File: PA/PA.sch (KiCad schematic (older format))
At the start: 80 parts, among them J1 Conn_Coaxial, J2 Conn_01x02, J27 Conn_01x01, J28 Conn_01x01, J3 Conn_Coaxial, J4 Conn_01x02, J5 Conn_01x02, J6 Conn_01x01, J7 Conn_01x01, J8 Conn_01x01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

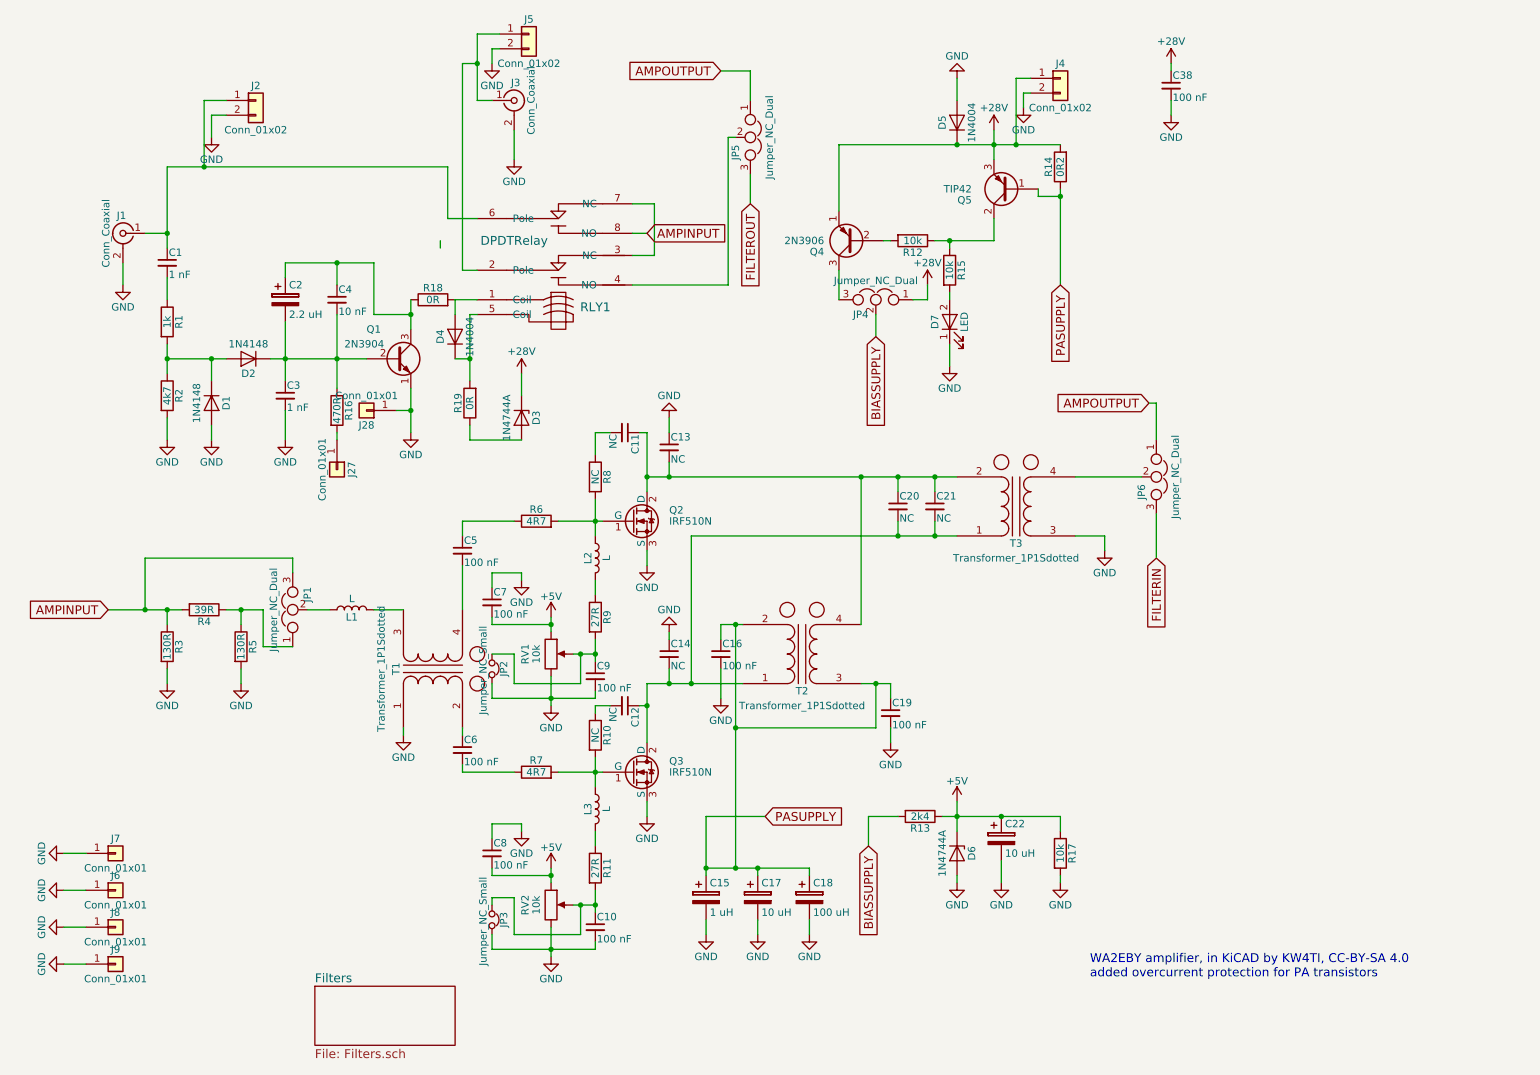
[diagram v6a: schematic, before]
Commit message: JLCPCB order tested
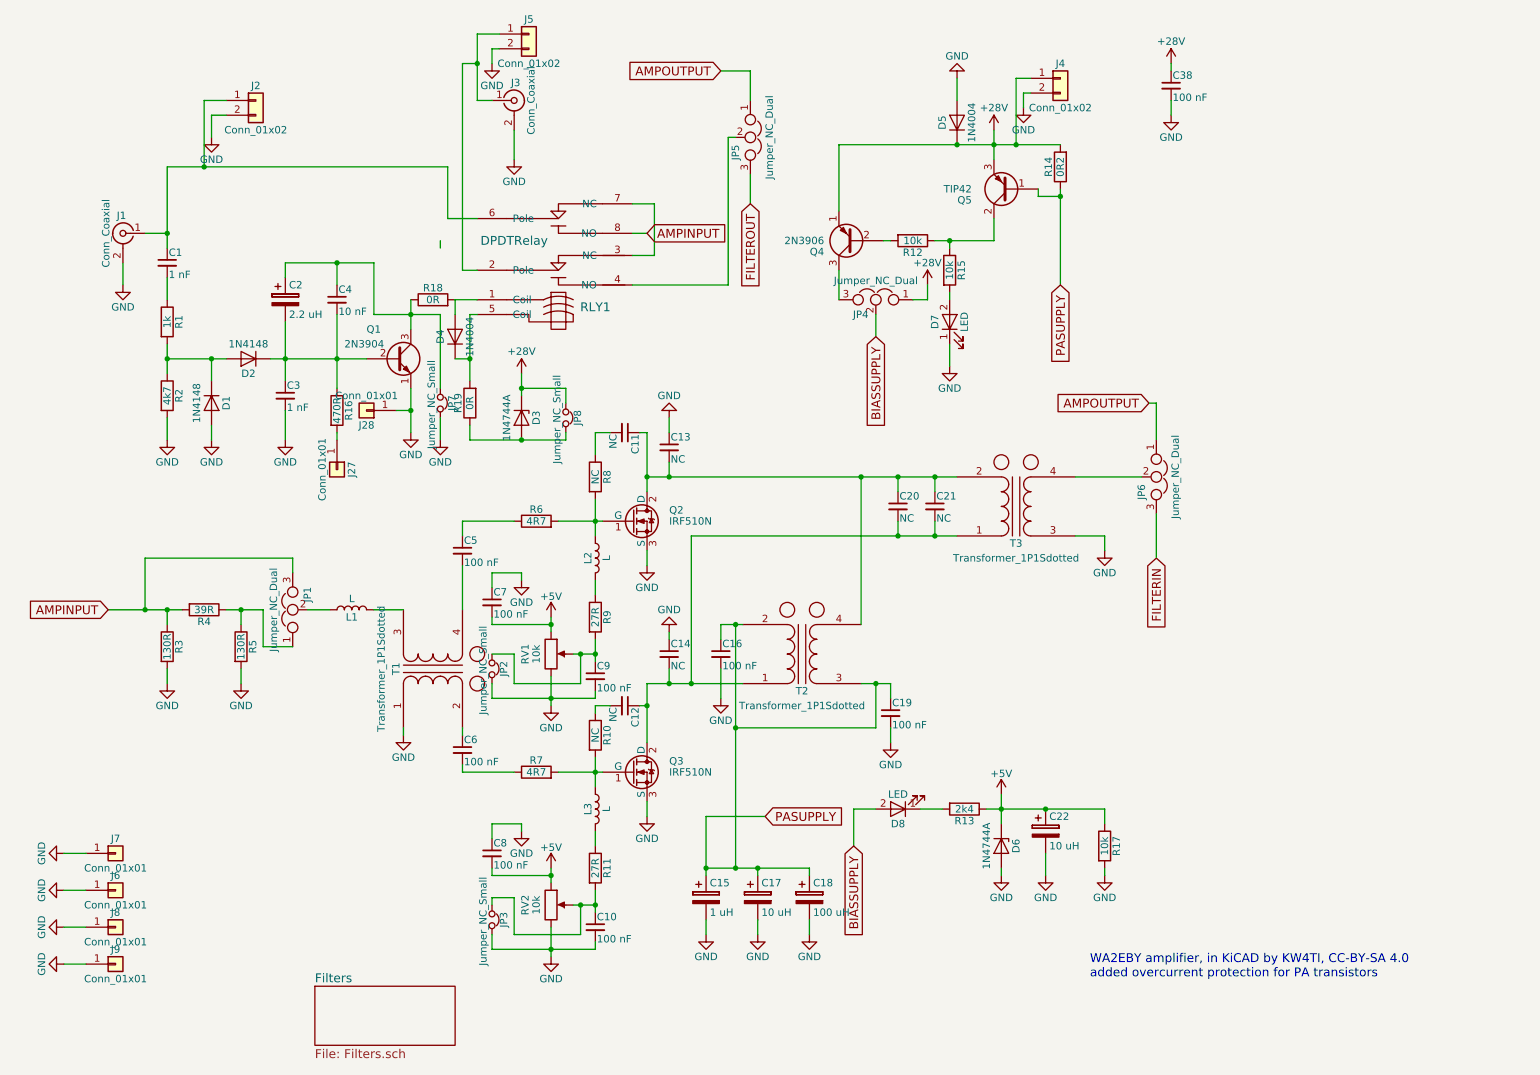
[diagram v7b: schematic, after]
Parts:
- added D8: LED, LEDs:LED_D3.0mm, symbol LED
- added JP7, JP8: Jumper_NC_Small, Pin_Headers:Pin_Header_Straight_1x02_Pitch2.54mm, symbol Jumper_NC_Small
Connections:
- net +28V: now also JP8.1
- net BIASSUPPLY: now also D8.2 (A); no longer R13.2
- net GND: now also JP7.2
- net at C2.1, C4.1, Q1.3 (C)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: now also JP7.1
- net at D3.2 (A), R19.1: now also JP8.2
- new net: D8.1 (K), R13.2
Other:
- moved on the sheet: C22, D6, R13, R17

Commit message: Fixed polarity of rig RXTX relay grounding
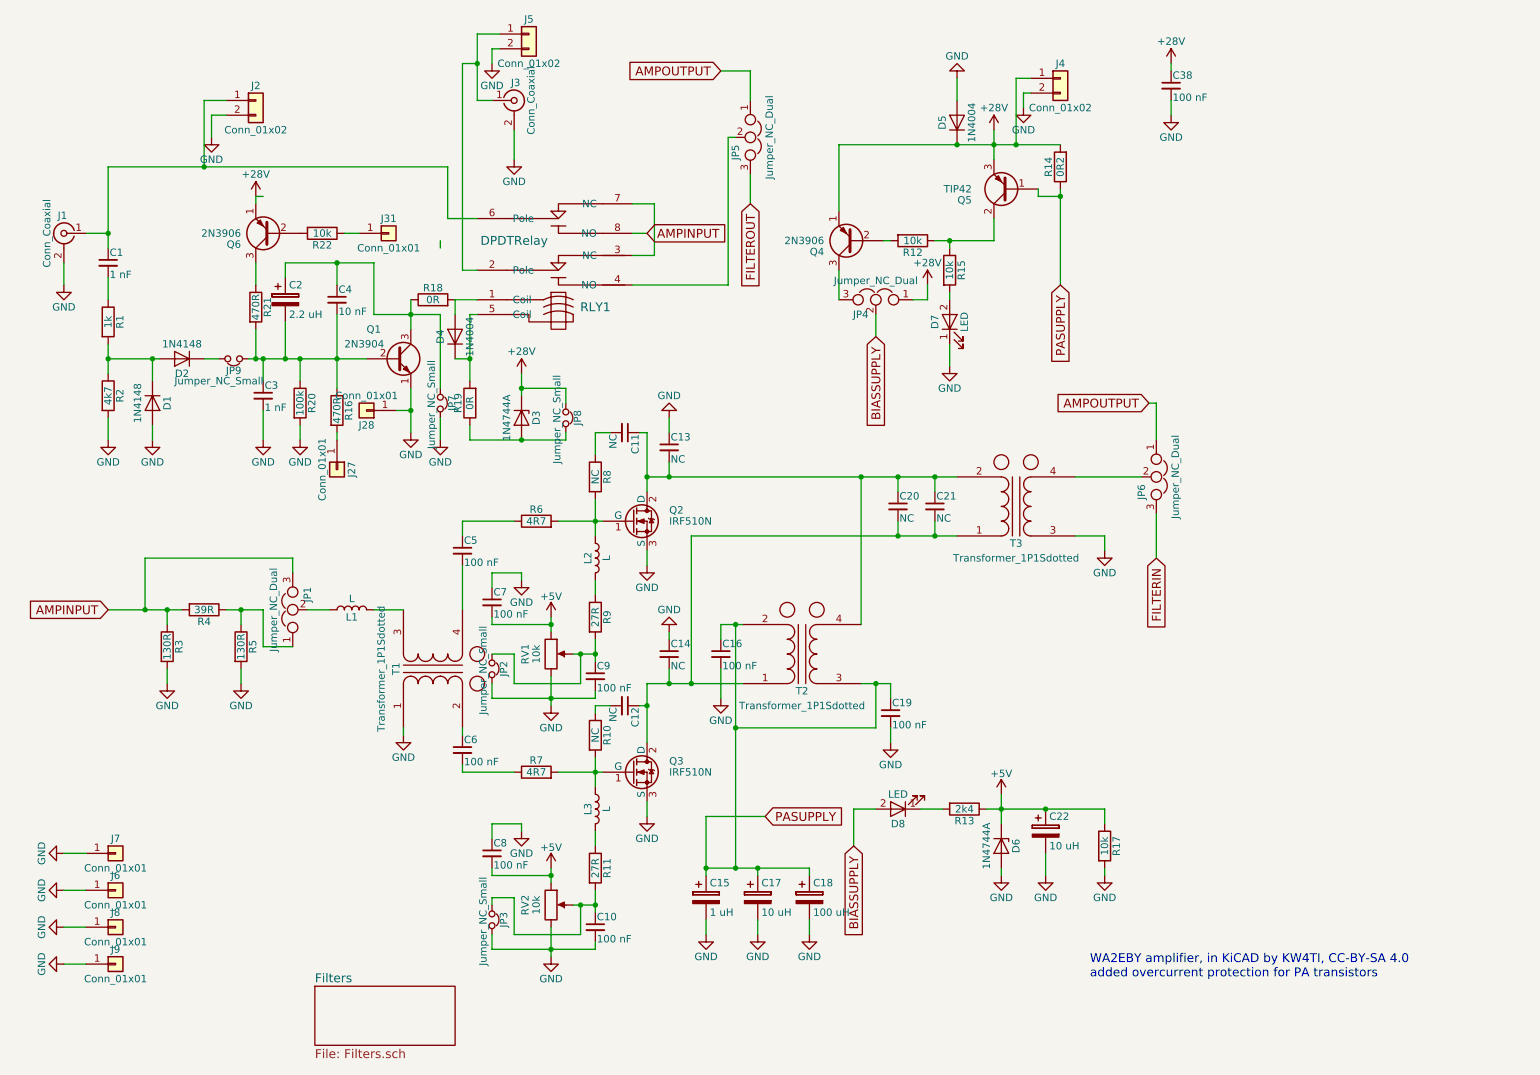
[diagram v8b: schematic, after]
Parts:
- added J31: Conn_01x01, Connectors:1pin, symbol Conn_01x01
- added JP9: Jumper_NC_Small, Pin_Headers:Pin_Header_Straight_1x02_Pitch2.54mm, symbol Jumper_NC_Small
- added Q6: 2N3906, TO_SOT_Packages_THT:TO-92_Molded_Narrow, symbol 2N3906
- added R20: 100k, Resistors_THT:R_Axial_DIN0207_L6.3mm_D2.5mm_P7.62mm_Horizontal, symbol R
- added R21: 470R, Resistors_THT:R_Axial_DIN0207_L6.3mm_D2.5mm_P7.62mm_Horizontal, symbol R
- added R22: 10k, Resistors_THT:R_Axial_DIN0207_L6.3mm_D2.5mm_P7.62mm_Horizontal, symbol R
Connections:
- net +28V: now also Q6.1 (E)
- net GND: now also R20.2
- net at C2.2, C3.1, C4.2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: now also JP9.1, R20.1, R21.2; no longer D2.1 (K)
- new net: D2.1 (K), JP9.2
- new net: Q6.2 (B), R22.2
- new net: Q6.3 (C), R21.1
- new net: J31.1 (Pin_1), R22.1
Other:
- moved on the sheet: C1, C3, D1, D2, J1, R1, R2
